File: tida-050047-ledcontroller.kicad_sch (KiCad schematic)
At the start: 139 parts, among them Q1 AOD424, Q2 AOD424, U1 TPS25750DRJKR, U10 XT30PW-F, U11 HY2213-BB3A, U12 HY2213-BB3A, U13 AP2300-ES, U14 AP2300-ES, U15 SB1045L_C2844167, U16 BQ7790400PWR, U17 SMTSO3015CTJ, U18 SMTSO3015CTJ, U19 SMTSO3015CTJ, U2 CAT24C256WI-GT3, U20 SMTSO3015CTJ, U21 BQ25798RQMR, U3 TLV75533PDBVR, U4 TPS54531DDAR, U6 HY2213-BB3A, U7 HY2213-BB3A, U8 AP2300-ES, U9 AP2300-ES

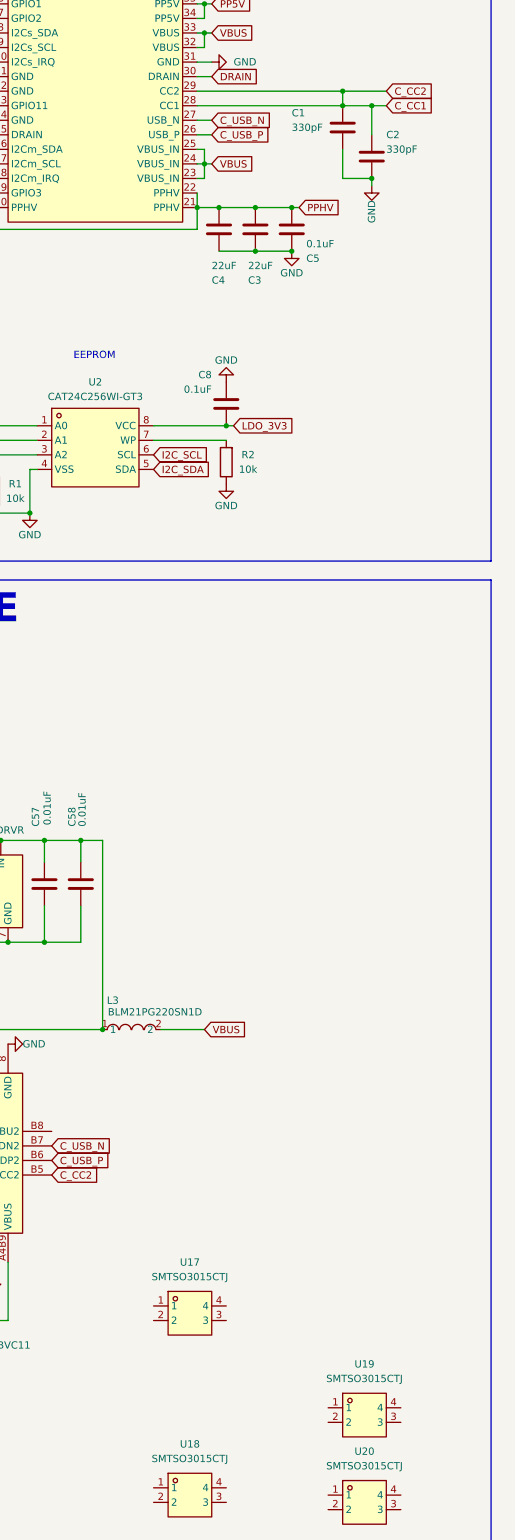
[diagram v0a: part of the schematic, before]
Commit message: fix zones with via stiching
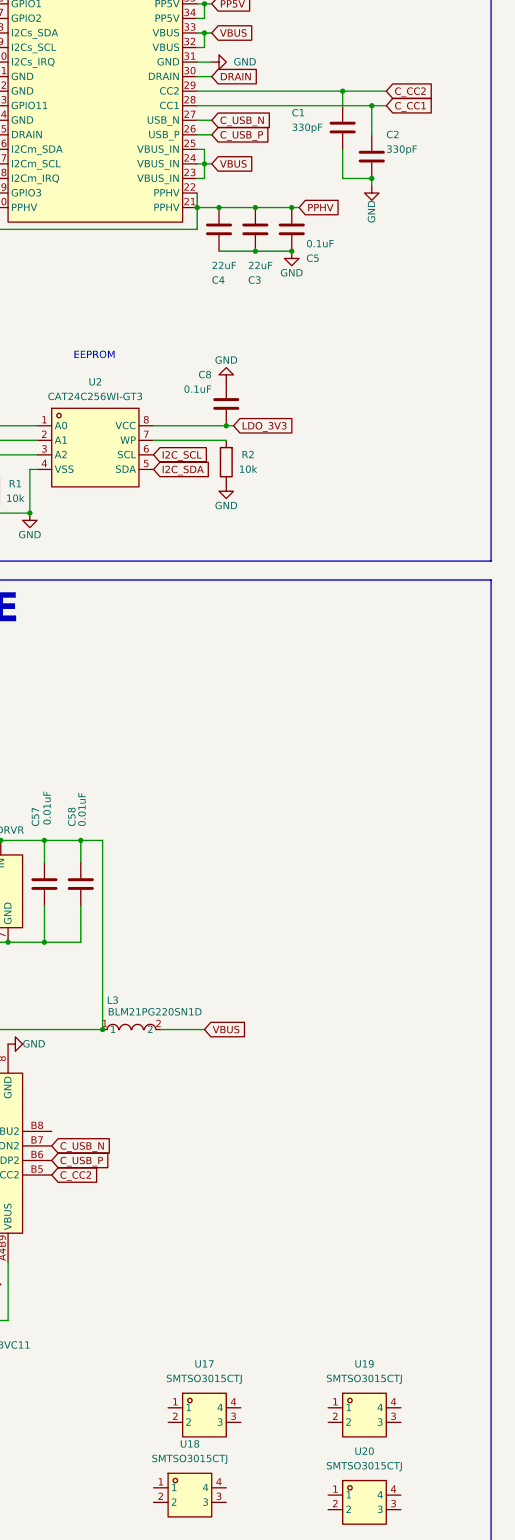
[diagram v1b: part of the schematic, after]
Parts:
- C30, C41: footprint Capacitor_SMD:C_0603_1608Metric_Pad1.08x0.95mm_HandSolder -> Capacitor_SMD:C_0402_1005Metric_Pad0.74x0.62mm_HandSolder
- U17, U18, U19, U20: footprint easyeda2kicad:SMD_BD5.6-L5.6-W5.6-D4.1 -> easyeda2kicad:SMTSO3030CTJ
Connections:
- net C_CC1: no longer C1.1, U1.29 (CC2), USB1.B5 (CC2)
- new net C_CC2: C1.1, U1.29 (CC2), USB1.B5 (CC2)
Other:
- moved on the sheet: U17
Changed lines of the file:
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@@
 	)
 	(junction
-		(at 181.61 91.44)
-		(diameter 0)
-		(color 0 0 0 0)
-	)
-	(junction
 		(at 359.41 287.02)
 		(diameter 0)
@@
 	(wire
 		(pts
-			(xy 181.61 91.44) (xy 186.69 91.44)
+			(xy 156.21 91.44) (xy 186.69 91.44)
 		)
 		(stroke
@@
 	(wire
 		(pts
-			(xy 156.21 91.44) (xy 181.61 91.44)
-		)
-		(stroke
-			(width 0)
-			(type default)
-		)
-	)
-	(wire
-		(pts
 			(xy 157.48 81.28) (xy 157.48 78.74)
 		)
@@
 			)
 		)
-		(property "Footprint" "easyeda2kicad:SMD_BD5.6-L5.6-W5.6-D4.1"
+		(property "Footprint" "easyeda2kicad:SMTSO3030CTJ"
 			(at 154.94 342.9 0)
 			(effects
@@
 			)
 		)
-		(property "Footprint" "Capacitor_SMD:C_0603_1608Metric_Pad1.08x0.95mm_HandSolder"
+		(property "Footprint" "Capacitor_SMD:C_0402_1005Metric_Pad0.74x0.62mm_HandSolder"
 			(at 348.2848 173.99 0)
 			(effects
@@
 			)
 		)
-		(property "Footprint" "Capacitor_SMD:C_0603_1608Metric_Pad1.08x0.95mm_HandSolder"
+		(property "Footprint" "Capacitor_SMD:C_0402_1005Metric_Pad0.74x0.62mm_HandSolder"
 			(at 296.8752 181.61 0)
 			(effects
@@
 			)
 		)
-		(property "Footprint" "easyeda2kicad:SMD_BD5.6-L5.6-W5.6-D4.1"
+		(property "Footprint" "easyeda2kicad:SMTSO3030CTJ"
 			(at 185.42 328.93 0)
 			(effects
@@
 			)
 		)
-		(property "Footprint" "easyeda2kicad:SMD_BD5.6-L5.6-W5.6-D4.1"
+		(property "Footprint" "easyeda2kicad:SMTSO3030CTJ"
 			(at 185.42 344.17 0)
 			(effects
@@
 	(symbol
 		(lib_id "easyeda2kicad:SMTSO3015CTJ")
-		(at 154.94 302.26 0)
+		(at 157.48 320.04 0)
 		(unit 1)
 		(exclude_from_sim no)
@@
 		(fields_autoplaced yes)
 		(property "Reference" "U17"
-			(at 154.94 293.37 0)
+			(at 157.48 311.15 0)
 			(effects
 				(font
@@
 		)
 		(property "Value" "SMTSO3015CTJ"
-			(at 154.94 295.91 0)
+			(at 157.48 313.69 0)
 			(effects
 				(font
@@
 			)
 		)
-		(property "Footprint" "easyeda2kicad:SMD_BD5.6-L5.6-W5.6-D4.1"
-			(at 154.94 311.15 0)
+		(property "Footprint" "easyeda2kicad:SMTSO3030CTJ"
+			(at 157.48 328.93 0)
 			(effects
 				(font
@@
 		)
 		(property "Datasheet" ""
-			(at 154.94 302.26 0)
+			(at 157.48 320.04 0)
 			(effects
 				(font
@@
 		)
 		(property "Description" ""
-			(at 154.94 302.26 0)
+			(at 157.48 320.04 0)
 			(effects
 				(font
@@
 		)
 		(property "LCSC Part" "C2915632"
-			(at 154.94 313.69 0)
+			(at 157.48 331.47 0)
 			(effects
 				(font

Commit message: delete cell balancing for parallel desing
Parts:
- removed C11, C12, C13, C14: 100nF, Capacitor_SMD:C_0603_1608Metric_Pad1.08x0.95mm_HandSolder, symbol Device:C
- removed H2: DZ254R-11-04-63, easyeda2kicad:HDR-TH_4P-P2.54-V-M, symbol easyeda2kicad:DZ254R-11-04-63
- removed JP1, JP2, JP3, JP4: SolderJumper_2_Bridged, Jumper:SolderJumper-2_P1.3mm_Bridged_RoundedPad1.0x1.5mm, symbol Jumper:SolderJumper_2_Bridged
- removed R17, R18, R21, R22: 100R, Resistor_SMD:R_0603_1608Metric_Pad0.98x0.95mm_HandSolder, symbol Device:R
- removed R19, R20, R23, R24: 100R, Resistor_SMD:R_1210_3225Metric_Pad1.30x2.65mm_HandSolder, symbol Device:R
- removed U11, U12, U6, U7: HY2213-BB3A, easyeda2kicad:SOT-23-6_L2.9-W1.6-P0.95-LS2.8-BR, symbol easyeda2kicad:HY2213-BB3A
- removed U13, U14, U8, U9: AP2300-ES, easyeda2kicad:SOT-23-3_L2.9-W1.3-P1.90-LS2.4-BR, symbol easyeda2kicad:AP2300-ES
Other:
- note added: "Power"
- note added: "SMD nuts"
- note added: "USB-C power delivery (PD) controller"
- note removed: "I2C for Internat Debug"
- note removed: "Not on board"
- note removed: "Power 5V TO 3.3V"
- note removed: "USB-C and power delivery (PD) controller"
- moved on the sheet: U17, U18, U19, U20

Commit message: add pcb layout using the layout guidelines froms the texas instruments ICs
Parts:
- added C11: OVZ101M1CTR-0606, easyeda2kicad:CAP-SMD_BD6.3-L6.6-W6.6-FD-A, symbol easyeda2kicad:OVZ101M1CTR-0606
- added H2, H7: PZ254V-11-02P, easyeda2kicad:HDR-TH_2P-P2.54-V-M, symbol easyeda2kicad:PZ254V-11-02P
- added R17: 30.31k, Resistor_SMD:R_0603_1608Metric_Pad0.98x0.95mm_HandSolder, symbol Device:R
- added R18: 5.24k, Resistor_SMD:R_0603_1608Metric_Pad0.98x0.95mm_HandSolder, symbol Device:R
- added TH1: 10k, symbol Device:Thermistor
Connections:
- net REGN is gone; now on net ILIM_HIZ: C36.2, U21.5 (REGN)
- net +BATT: now also H2.2
- net GND: now also U17.1, U17.2, U17.3, U17.4, U18.1, U18.2, U18.3, U18.4, U19.1, U19.2, U19.3, U19.4, U20.1, U20.2, U20.3, U20.4, USB1.B1A12 (GND), C11.2, H2.1, H7.1, R17.2, TH1.2; no longer USB1.8 (GND)
- net ILIM_HIZ: now also R18.1
- net PP5V: now also H7.2
- net SYS: now also C11.1
- new net: R17.1, R18.2, TH1.1
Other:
- note added: "For maximum charging current"
- moved on the sheet: LED1, R14

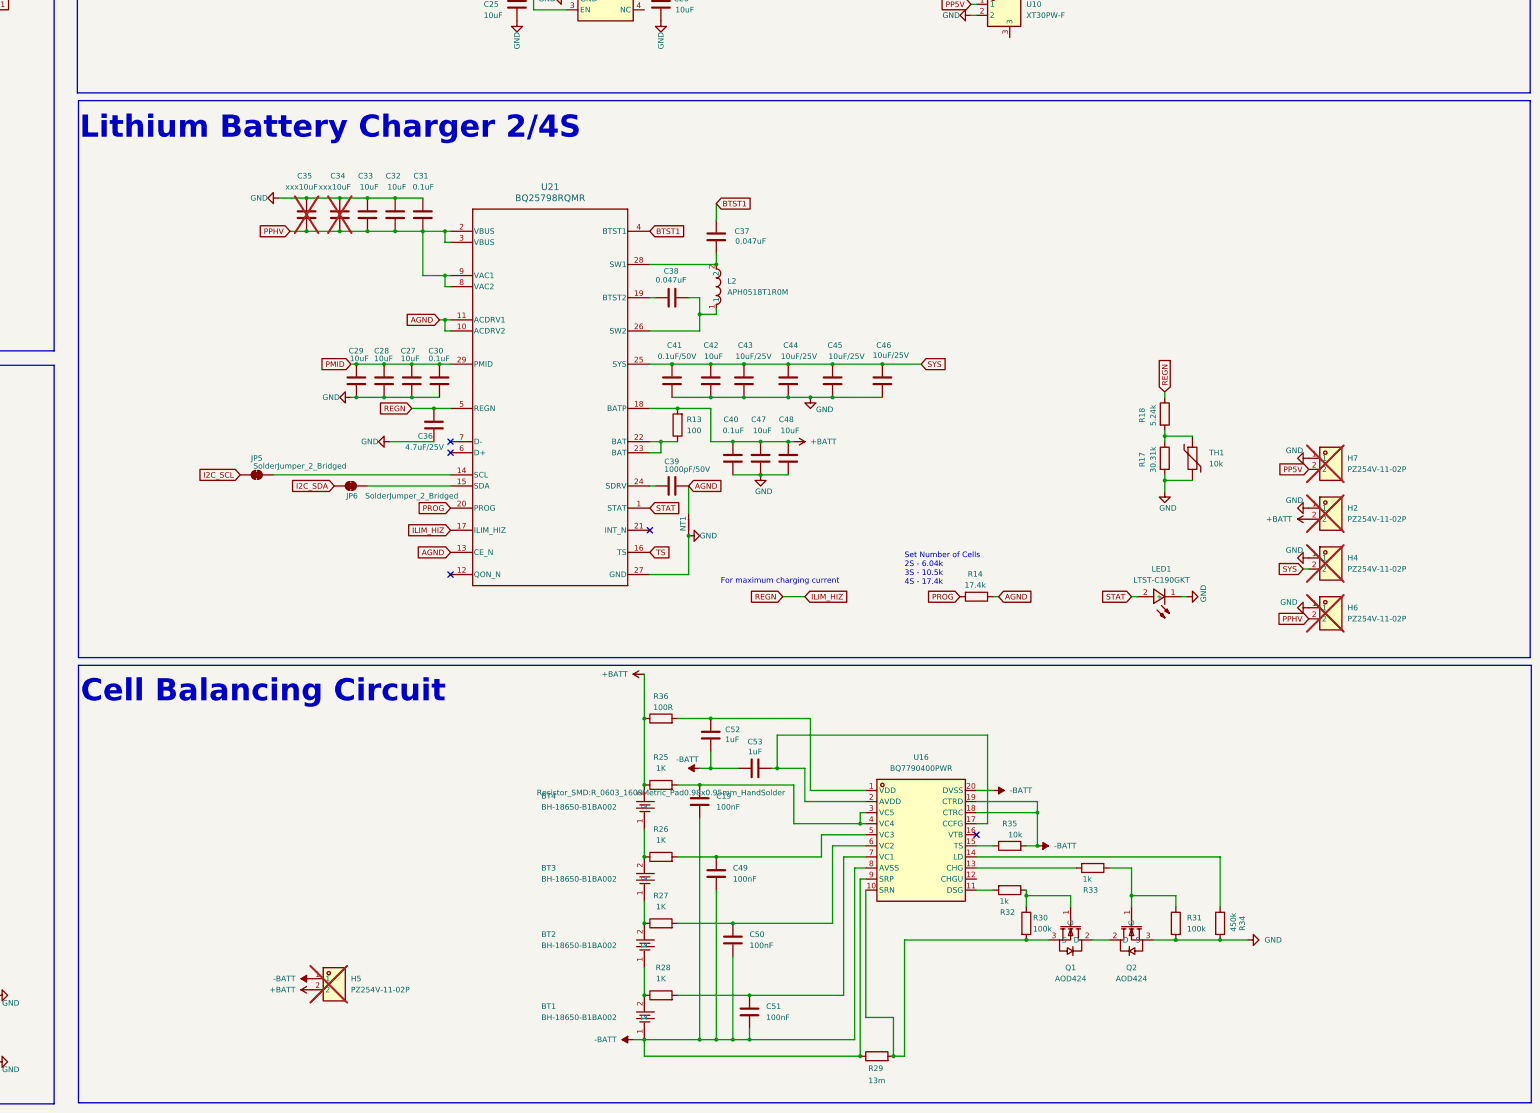
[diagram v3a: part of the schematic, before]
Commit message: replace battery protection with IC that actually balances the cells
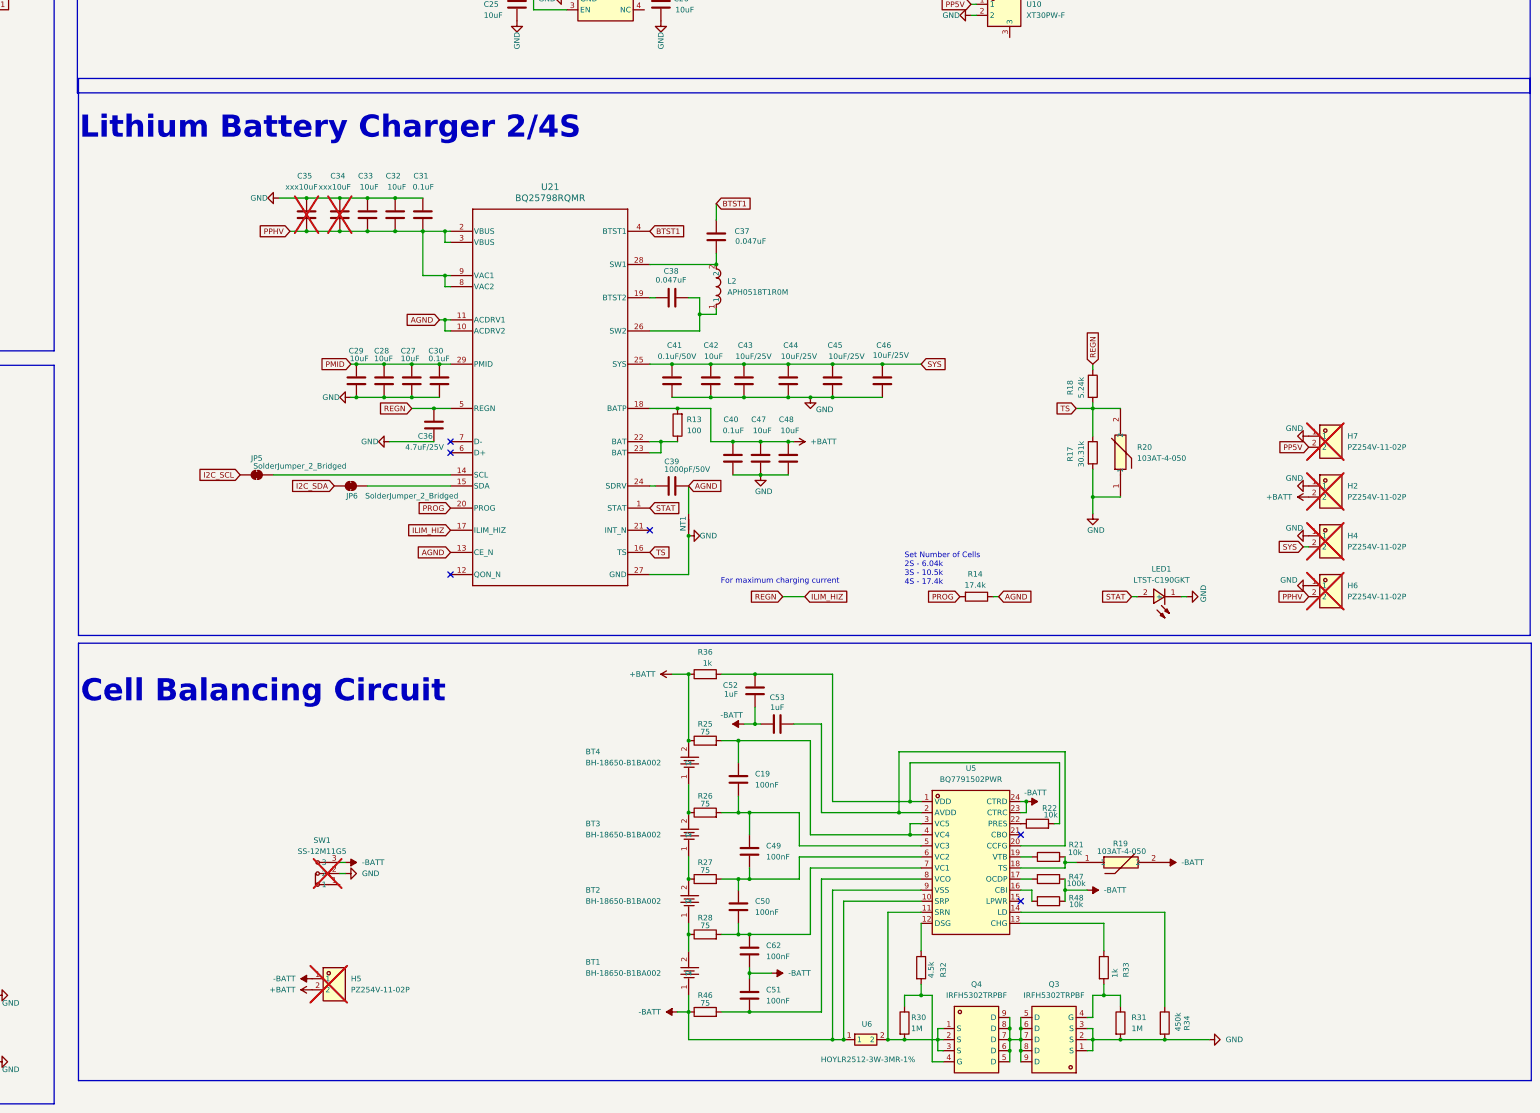
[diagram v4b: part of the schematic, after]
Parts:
- removed Q1, Q2: AOD424, easyeda2kicad:TO-252-3_L6.5-W6.1-P4.58-LS9.9-BR, symbol easyeda2kicad:AOD424
- removed R29: 13m, Resistor_SMD:R_1206_3216Metric_Pad1.30x1.75mm_HandSolder, symbol Device:R
- removed R35: 10k, Resistor_SMD:R_0603_1608Metric_Pad0.98x0.95mm_HandSolder, symbol Device:R
- removed TH1: 10k, symbol Device:Thermistor
- removed U16: BQ7790400PWR, easyeda2kicad:TSSOP-20_L6.5-W4.4-P0.65-LS6.4-BL, symbol easyeda2kicad:BQ7790400PWR
- added C62: 100nF, Capacitor_SMD:C_0603_1608Metric_Pad1.08x0.95mm_HandSolder, symbol Device:C
- added Q3, Q4: IRFH5302TRPBF, easyeda2kicad:PQFN-8_L6.0-W5.0-P1.27-LS6.0-BL, symbol easyeda2kicad:IRFH5302TRPBF
- added R19, R20: 103AT-4-050, easyeda2kicad:RES-TH_L2.5-W2.5-P1.70-D0.3, symbol easyeda2kicad:103AT-4-050
- added R21, R22, R48: 10k, Resistor_SMD:R_0603_1608Metric_Pad0.98x0.95mm_HandSolder, symbol Device:R
- added R46: 75, Resistor_SMD:R_1206_3216Metric_Pad1.30x1.75mm_HandSolder, symbol Device:R
- added R47: 100k, Resistor_SMD:R_0603_1608Metric_Pad0.98x0.95mm_HandSolder, symbol Device:R
- added SW1: SS-12M11G5, easyeda2kicad:SW-TH_XKB_SS-12M11XX, symbol easyeda2kicad:SS-12M11G5
- added U5: BQ7791502PWR, easyeda2kicad:TSSOP-24_L7.8-W4.4-P0.65-LS6.4-BL_1, symbol easyeda2kicad:BQ7791502PWR
- added U6: HOYLR2512-3W-3MR-1%, easyeda2kicad:R2512, symbol easyeda2kicad:HOYLR2512-3W-3MR-1%
- R25, R26, R27, R28: value 1K -> 75; footprint Resistor_SMD:R_0603_1608Metric_Pad0.98x0.95mm_HandSolder -> Resistor_SMD:R_1206_3216Metric_Pad1.30x1.75mm_HandSolder
- R30, R31: value 100k -> 1M
- R32: value 1k -> 4.5k
- R36: value 100R -> 1k
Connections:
- net -BATT: now also C51.1, C62.2, R19.2, R46.1, R47.1, R48.1, SW1.3, U5.10 (SRP), U5.23 (CTRC), U5.24 (CTRD), U5.9 (VSS), U6.1; no longer C19.2, C49.2, C50.2, C51.2
- net GND: now also Q3.1 (S), Q3.2 (S), Q3.3 (S), R20.1, SW1.2
- net TS: now also R17.1, R18.2, R20.2
- net at R30.2: now also Q4.1 (S), Q4.2 (S), Q4.3 (S), U5.11 (SRN), U6.2
- net at C49.1, R26.2: now also C19.2, U5.5 (VC3)
- net at R30.1: now also R32.2, Q4.4 (G); no longer R32.1
- net at R33.1: now also U5.13 (CHG); no longer R31.1
- net at R33.2: now also R31.1, Q3.4 (G)
- net at C50.1, R27.2: now also C49.2, U5.6 (VC2)
- net at R28.2: now also C50.2, C62.1, U5.7 (VC1); no longer C51.1
- net at C19.1, R25.2: now also U5.3 (VC5), U5.4 (VC4)
- net at C52.2, R36.2: now also R22.2, U5.1 (VDD)
- net at R34.1: now also U5.14 (LD)
- net at C53.2: now also U5.2 (AVDD), U5.20 (CCFG)
- new net: R47.2, U5.17 (OCDP)
- new net: C51.2, R46.2, U5.8 (VCO)
- new net: R21.1, U5.19 (VTB)
- new net: R19.1, R21.2, U5.18 (TS)
- new net: R22.1, U5.22 (PRES)
- new net: R48.2, U5.16 (CBI)
- new net: R32.1, U5.12 (DSG)
- new net: Q3.5 (D), Q3.6 (D), Q3.7 (D), Q3.8 (D), Q3.9 (D), Q4.5 (D), Q4.6 (D), Q4.7 (D), Q4.8 (D), Q4.9 (D)
- no-connect marks 10 -> 11
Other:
- moved on the sheet: BT1, BT2, BT3, BT4, C19, C49, C50, C51, C52, C53, H2, H4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
